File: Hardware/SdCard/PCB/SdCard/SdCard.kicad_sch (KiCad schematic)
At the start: 7 parts, among them J1 Conn_01x08_Male, J2 Conn_01x08_Male

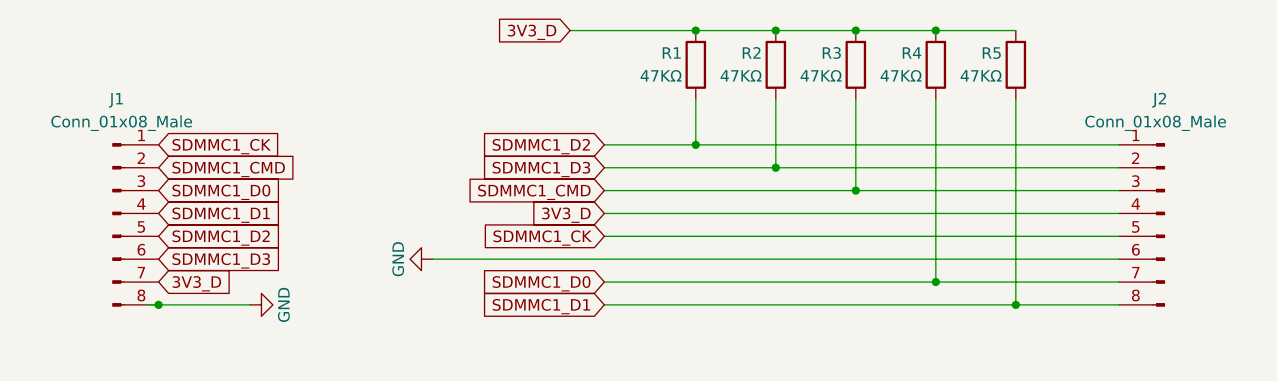
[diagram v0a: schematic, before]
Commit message: Edges removed
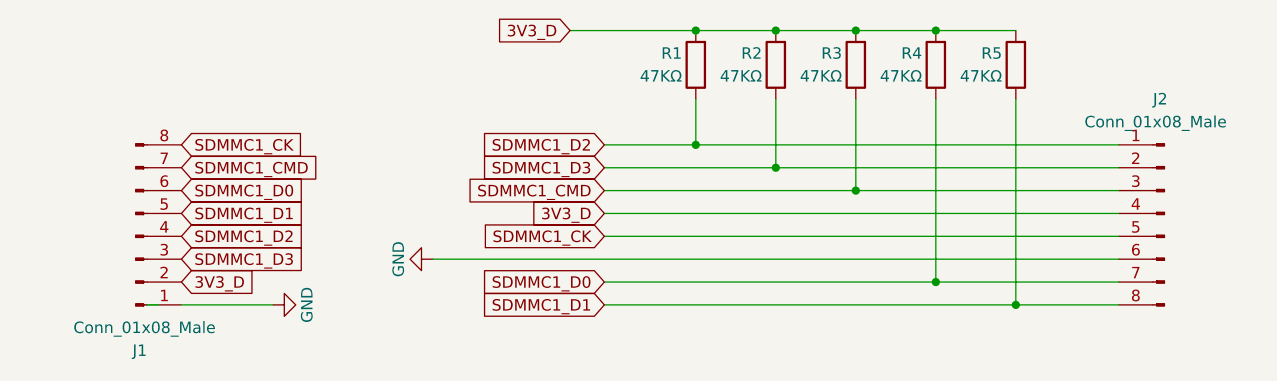
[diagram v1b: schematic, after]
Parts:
- J1: footprint Connector_PinSocket_2.54mm:PinSocket_1x08_P2.54mm_Vertical -> Connector_PinHeader_2.54mm:PinHeader_1x08_P2.54mm_Horizontal
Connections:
- net 3V3_D: now also J1.2 (Pin_2); no longer J1.7 (Pin_7)
- net GND: now also J1.1 (Pin_1); no longer J1.8 (Pin_8)
- net SDMMC1_CK: now also J1.8 (Pin_8); no longer J1.1 (Pin_1)
- net SDMMC1_CMD: now also J1.7 (Pin_7); no longer J1.2 (Pin_2)
- net SDMMC1_D0: now also J1.6 (Pin_6); no longer J1.3 (Pin_3)
- net SDMMC1_D1: now also J1.5 (Pin_5); no longer J1.4 (Pin_4)
- net SDMMC1_D2: now also J1.4 (Pin_4); no longer J1.5 (Pin_5)
- net SDMMC1_D3: now also J1.3 (Pin_3); no longer J1.6 (Pin_6)
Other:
- moved on the sheet: J1
